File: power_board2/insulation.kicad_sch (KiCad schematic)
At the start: 13 parts, among them IC2 PJ-002A, J1 UJC-HP-3-SMT-TR

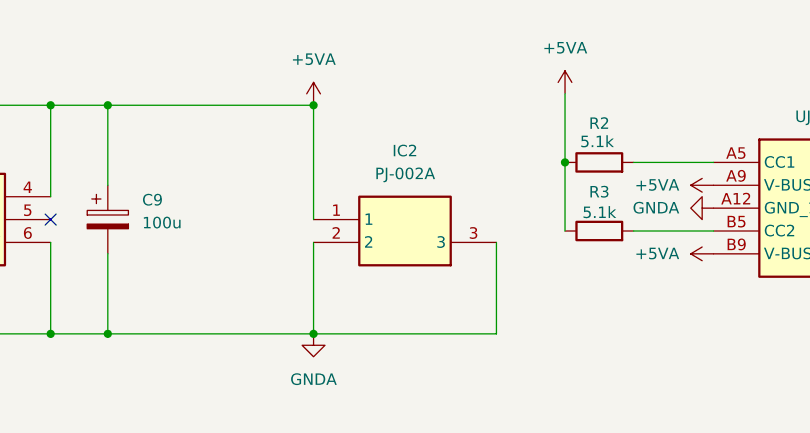
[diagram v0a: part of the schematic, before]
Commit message: 非常停止スイッチを追加
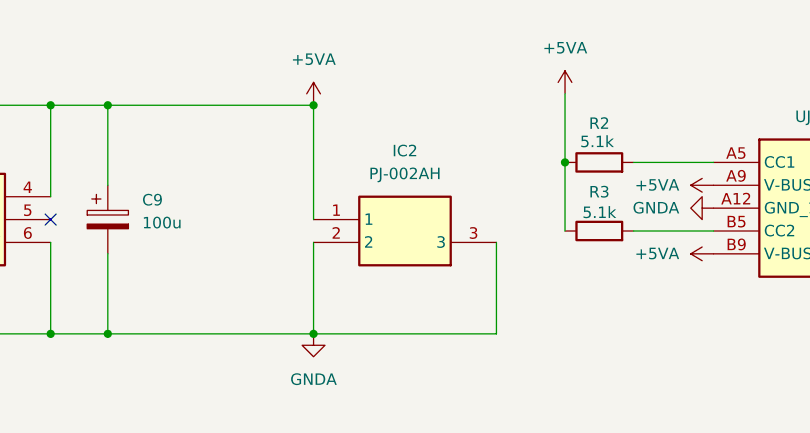
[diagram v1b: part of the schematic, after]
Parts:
- IC2: value PJ-002A -> PJ-002AH; footprint power_board2:PJ002A -> power_board2:PJ002AH
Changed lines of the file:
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@@
 			)
 		)
-		(property "Value" "PJ-002A"
+		(property "Value" "PJ-002AH"
 			(at 156.21 43.18 0)
 			(effects
@@
 			)
 		)
-		(property "Footprint" "power_board2:PJ002A"
+		(property "Footprint" "power_board2:PJ002AH"
 			(at 149.86 -44.12 0)
 			(effects
